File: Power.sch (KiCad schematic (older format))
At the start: 22 parts, among them J14 Conn_01x02, J16 Conn_01x02, U2 SPV1040, U4 TPS62130

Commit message: Finalize schematic
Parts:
- J14, J16: footprint Connector_JST:JST_XH_B2B-XH-AM_1x02_P2.50mm_Vertical -> Connector_JST:JST_XH_S2B-XH-A_1x02_P2.50mm_Horizontal
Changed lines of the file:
@@
 F 0 "J16" H 3318 4825 50  0000 C CNN
 F 1 "Conn_01x02" H 3318 4916 50  0000 C CNN
-F 2 "Connector_JST:JST_XH_B2B-XH-AM_1x02_P2.50mm_Vertical" H 3400 5150 50  0001 C CNN
+F 2 "Connector_JST:JST_XH_S2B-XH-A_1x02_P2.50mm_Horizontal" H 3400 5150 50  0001 C CNN
 F 3 "~" H 3400 5150 50  0001 C CNN
 	1    3400 5150
@@
 F 0 "J14" H 3468 1125 50  0000 C CNN
 F 1 "Conn_01x02" H 3468 1216 50  0000 C CNN
-F 2 "Connector_JST:JST_XH_B2B-XH-AM_1x02_P2.50mm_Vertical" H 3550 1450 50  0001 C CNN
+F 2 "Connector_JST:JST_XH_S2B-XH-A_1x02_P2.50mm_Horizontal" H 3550 1450 50  0001 C CNN
 F 3 "~" H 3550 1450 50  0001 C CNN
 	1    3550 1450

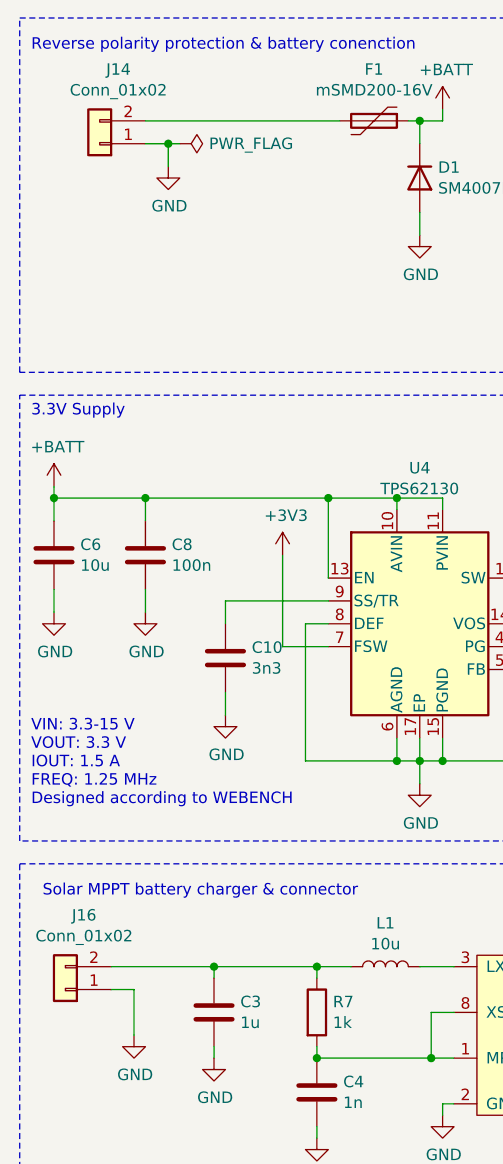
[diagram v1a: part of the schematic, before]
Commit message: Finish routing of Rev 1
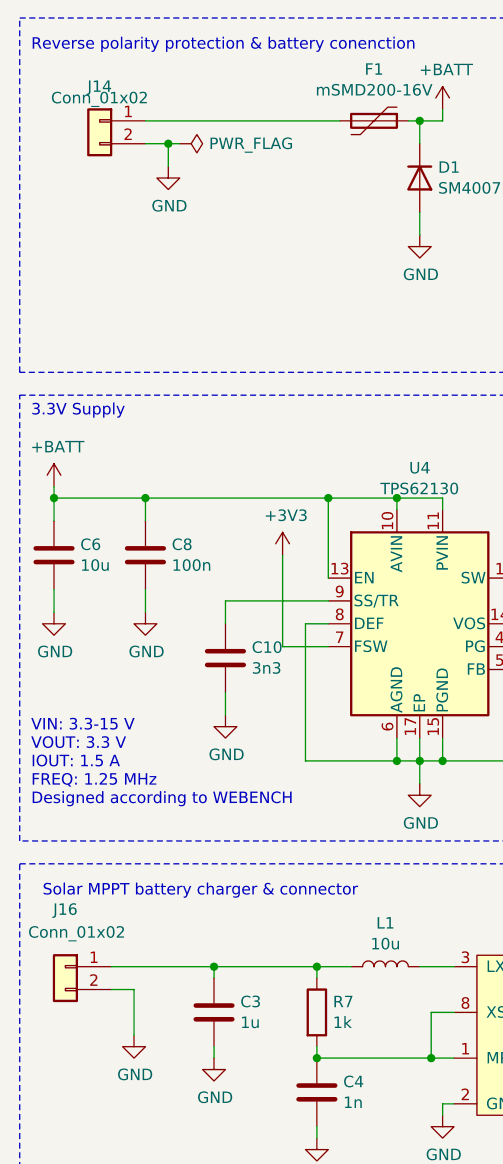
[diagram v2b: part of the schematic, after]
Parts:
- J14, J16: footprint Connector_JST:JST_XH_S2B-XH-A_1x02_P2.50mm_Horizontal -> Connector_JST:JST_XH_B2B-XH-AM_1x02_P2.50mm_Vertical
- L1: footprint (none) -> co2_sensor_node:MWSA0503S; LCSC (none) -> C408412
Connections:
- net GND: now also J14.2 (Pin_2), J16.2 (Pin_2); no longer J14.1 (Pin_1), J16.1 (Pin_1)
- net at F1.2: now also J14.1 (Pin_1); no longer J14.2 (Pin_2)
- net at C3.1, L1.1, R7.1: now also J16.1 (Pin_1); no longer J16.2 (Pin_2)
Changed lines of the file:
@@
 $Descr A4 11693 8268
 encoding utf-8
-Sheet 7 9
+Sheet 7 10
 Title ""
 Date ""
@@
 L Connector_Generic:Conn_01x02 J16
 U 1 1 60E02497
-P 3400 5150
-F 0 "J16" H 3318 4825 50  0000 C CNN
-F 1 "Conn_01x02" H 3318 4916 50  0000 C CNN
-F 2 "Connector_JST:JST_XH_S2B-XH-A_1x02_P2.50mm_Horizontal" H 3400 5150 50  0001 C CNN
-F 3 "~" H 3400 5150 50  0001 C CNN
-	1    3400 5150
-	-1   0    0    1
+P 3400 5050
+F 0 "J16" H 3400 5300 50  0000 C CNN
+F 1 "Conn_01x02" H 3350 5200 50  0000 C CNN
+F 2 "Connector_JST:JST_XH_B2B-XH-AM_1x02_P2.50mm_Vertical" H 3400 5050 50  0001 C CNN
+F 3 "~" H 3400 5050 50  0001 C CNN
+	1    3400 5050
+	-1   0    0    -1
 $EndComp
 Connection ~ 4500 5050
@@
 F 0 "L1" V 4990 5050 50  0000 C CNN
 F 1 "10u" V 4899 5050 50  0000 C CNN
-F 2 "" H 4800 5050 50  0001 C CNN
+F 2 "co2_sensor_node:MWSA0503S" H 4800 5050 50  0001 C CNN
 F 3 "~" H 4800 5050 50  0001 C CNN
+F 4 "C408412" H 4800 5050 50  0001 C CNN "LCSC"
 	1    4800 5050
 	0    -1   -1   0
@@
 L Connector_Generic:Conn_01x02 J14
 U 1 1 60B3C468
-P 3550 1450
-F 0 "J14" H 3468 1125 50  0000 C CNN
-F 1 "Conn_01x02" H 3468 1216 50  0000 C CNN
-F 2 "Connector_JST:JST_XH_S2B-XH-A_1x02_P2.50mm_Horizontal" H 3550 1450 50  0001 C CNN
-F 3 "~" H 3550 1450 50  0001 C CNN
-	1    3550 1450
-	-1   0    0    1
-$EndComp
-Wire Wire Line
+P 3550 1350
+F 0 "J14" H 3550 1500 50  0000 C CNN
+F 1 "Conn_01x02" H 3550 1450 50  0000 C CNN
+F 2 "Connector_JST:JST_XH_B2B-XH-AM_1x02_P2.50mm_Vertical" H 3550 1350 50  0001 C CNN
+F 3 "~" H 3550 1350 50  0001 C CNN
+	1    3550 1350
+	-1   0    0    -1
+$EndComp
+Wire Wire Line
